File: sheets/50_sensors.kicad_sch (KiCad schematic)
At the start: 0 parts

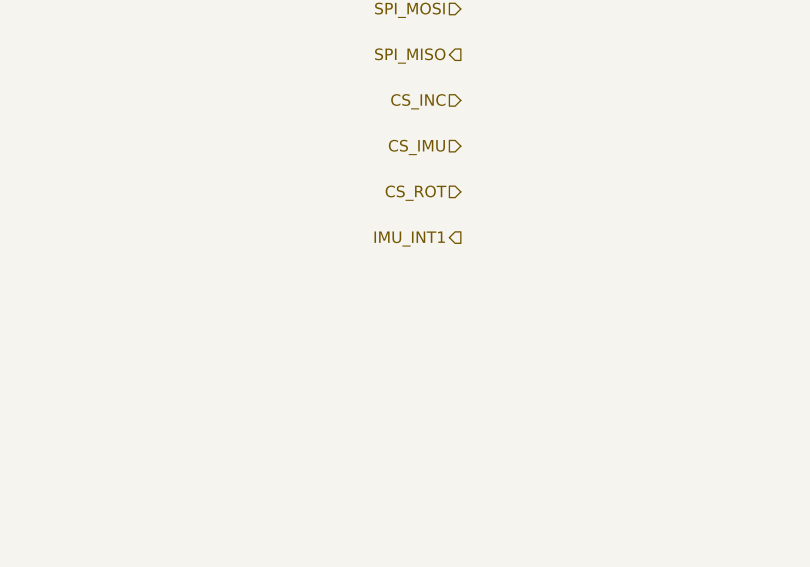
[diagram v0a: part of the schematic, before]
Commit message: Corrige la base del esquemático y añade reglas de proyecto
- Extrae el símbolo ADM3055E a lib/antmicro_adm3055ebriz.kicad_sym y lo
  registra en sym-lib-table con ${KIPRJMOD}.
- U1: huella Package_SO:SOIC-20W_7.5x12.8mm_P1.27mm (nota: verificar
  land pattern contra el datasheet).
- 10_power_input: power:GND -> GND_VEH; huellas y MPN de C1, C2 (0805
  X7R 100 V automotriz), C3 (EEE-HA2A470UP, 10x10) y F1 (1812, MPN
  pendiente).
- Nuevos pines jerárquicos CAN_SILENT (40_mcu -> 60_can, pull-down R1
  10k a GND_ISO) e IMU_INT2 (50_sensors -> 40_mcu).
- CLAUDE.md con reglas de librerías, campos, conexiones entre hojas,
  verificación por hoja y versión prototipo.
- Ignora output/ (reportes generados por kicad-mcp).

Co-Authored-By: Claude Opus 5.5 <noreply@anthropic.com>
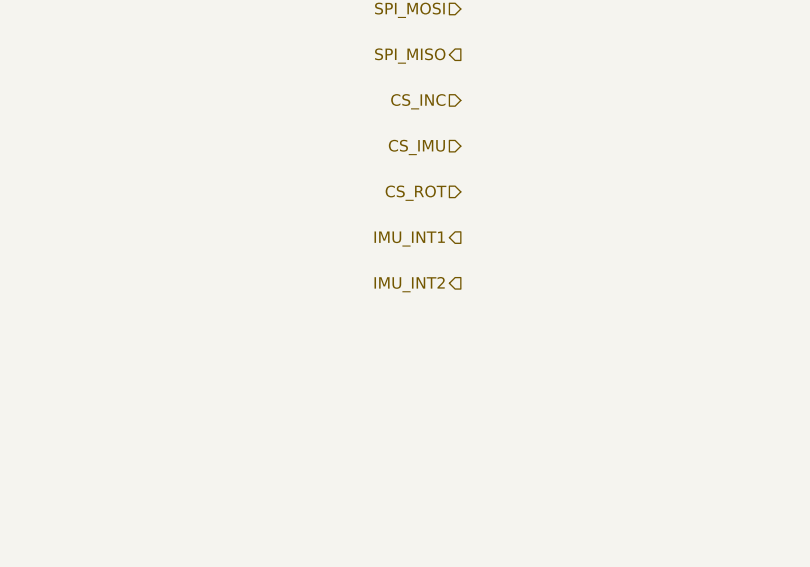
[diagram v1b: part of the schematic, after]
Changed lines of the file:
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@@
+		)
+	)
+	(hierarchical_label "IMU_INT2"
+		(shape output)
+		(at 238.76 66.04 180)
+		(effects
+			(font
+				(size 1.27 1.27)
+			)
+			(justify right)
 		)
 	)
